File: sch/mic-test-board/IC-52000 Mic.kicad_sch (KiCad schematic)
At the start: 5 parts

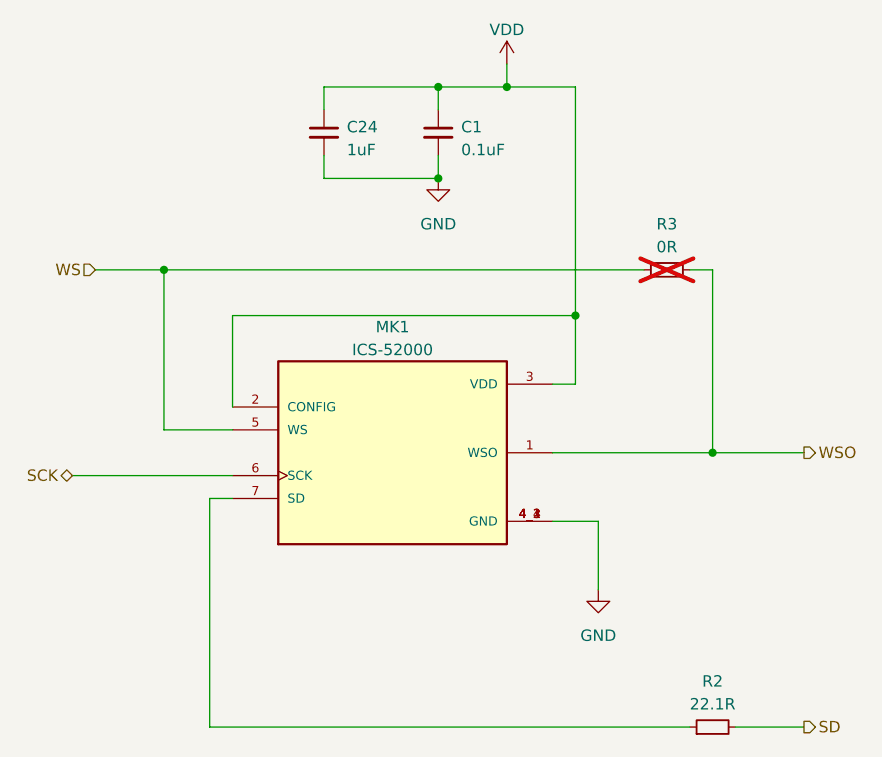
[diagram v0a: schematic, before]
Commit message: feat: schematic WIP
 - Analog front end 99% selected and wired up
 - uController/dev board interface 1% done
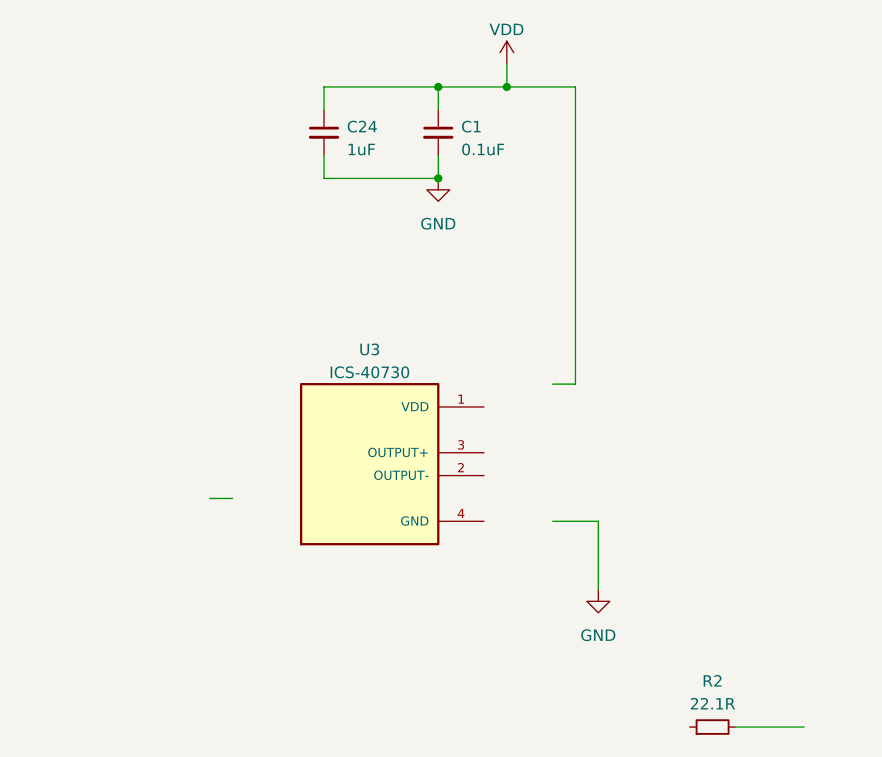
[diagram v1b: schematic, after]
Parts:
- removed MK1: ICS-52000, mic-test-board:MIC_ICS-52000, symbol mic-test-pcb:ICS-52000
- removed R3: 0R, Resistor_SMD:R_0603_1608Metric, symbol Device:R_Small
- added U3: ICS-40730, mic-test-board:MIC_ICS-40730, symbol mic-test-pcb:ICS-40730
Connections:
- net SD: no longer names the net of R2.2
